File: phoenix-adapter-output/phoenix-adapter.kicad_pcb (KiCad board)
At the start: 2 copper layers, 16.2 x 20 mm, 2 parts, among them CON101 RCJ-2223

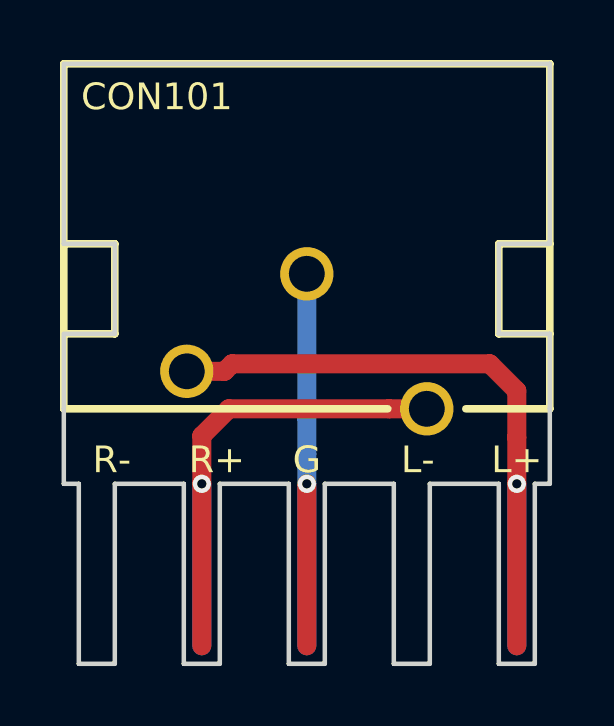
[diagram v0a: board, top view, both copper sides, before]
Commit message: Remove old gerbers, add jst gerbers
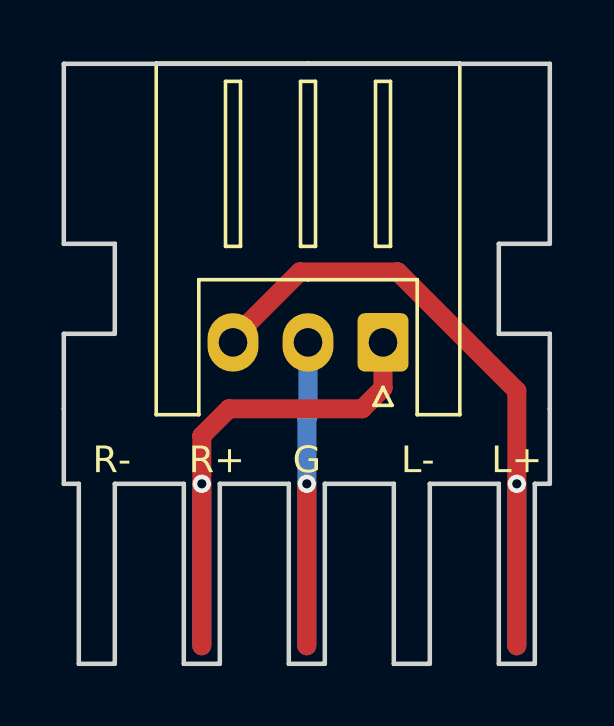
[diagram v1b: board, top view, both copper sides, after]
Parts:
- CON101: value RCJ-2223 -> JST-XH; footprint db-thparts:RCJ-2223 -> Connector_JST:JST_XH_S03B-XH-A_1x03_P2.50mm_Horizontal
- moved CON101 9.63 mm to (142.2, 116.6), turned to 180 degrees
- moved G*** 0.25 mm to (143.5, 109.2)
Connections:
- CON101 pad 1: GND -> /RIGHT
- CON101 pad 2: /LEFT -> GND
- CON101 pad 3: /RIGHT -> /LEFT
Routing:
- net GND: track 17.8 -> 15.5 mm
- net /LEFT: track 25.4 -> 26.0 mm
